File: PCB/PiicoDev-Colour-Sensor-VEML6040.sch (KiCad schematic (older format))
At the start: 23 parts, among them J1 , J2 , J3 Conn_PiicoDev_header_01x04_Ma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, J4 Conn_01x01_Male, Q1 BSS138, U1 VEML6040

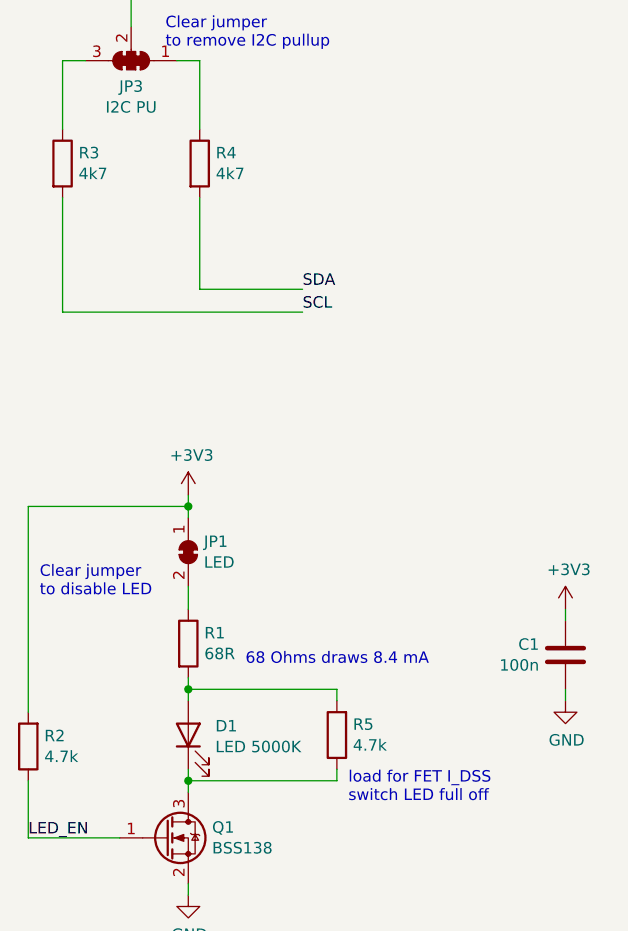
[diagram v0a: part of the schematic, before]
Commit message: Change 4k7 resistors to 10k
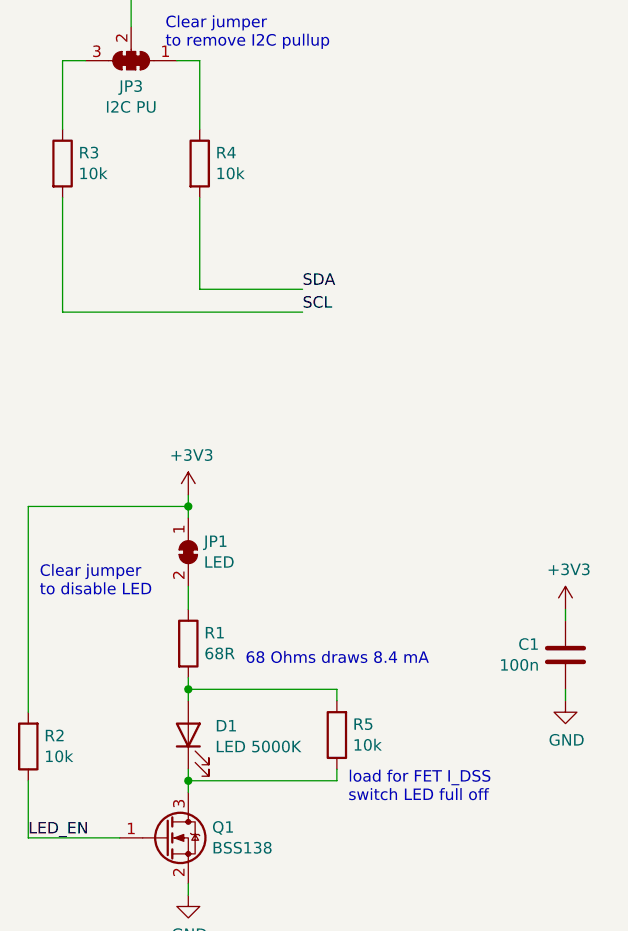
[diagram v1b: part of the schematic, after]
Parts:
- R2, R5: value 4.7k -> 10k
- R3, R4: value 4k7 -> 10k
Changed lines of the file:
@@
 P 2250 1600
 F 0 "R4" H 2320 1646 50  0000 L CNN
-F 1 "4k7" H 2320 1555 50  0000 L CNN
+F 1 "10k" H 2320 1555 50  0000 L CNN
 F 2 "Resistor_SMD:R_0402_1005Metric" V 2180 1600 50  0001 C CNN
 F 3 "~" H 2250 1600 50  0001 C CNN
@@
 P 1650 1600
 F 0 "R3" H 1720 1646 50  0000 L CNN
-F 1 "4k7" H 1720 1555 50  0000 L CNN
+F 1 "10k" H 1720 1555 50  0000 L CNN
 F 2 "Resistor_SMD:R_0402_1005Metric" V 1580 1600 50  0001 C CNN
 F 3 "~" H 1650 1600 50  0001 C CNN
@@
 P 1500 4150
 F 0 "R2" H 1430 4104 50  0000 R CNN
-F 1 "4.7k" H 1430 4195 50  0000 R CNN
+F 1 "10k" H 1430 4195 50  0000 R CNN
 F 2 "Resistor_SMD:R_0402_1005Metric" V 1430 4150 50  0001 C CNN
 F 3 "~" H 1500 4150 50  0001 C CNN
@@
 P 2850 4100
 F 0 "R5" H 2780 4054 50  0000 R CNN
-F 1 "4.7k" H 2780 4145 50  0000 R CNN
+F 1 "10k" H 2780 4145 50  0000 R CNN
 F 2 "Resistor_SMD:R_0402_1005Metric" V 2780 4100 50  0001 C CNN
 F 3 "~" H 2850 4100 50  0001 C CNN
